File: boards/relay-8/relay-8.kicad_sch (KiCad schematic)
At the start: 8 parts, among them J1 Screw_Terminal_01x02, J2 USB_B_Micro, J3 Screw_Terminal_01x02, SW1 SW_Push, U1 ESP32-WROOM-32D, U2 MCP2200-I-MQ

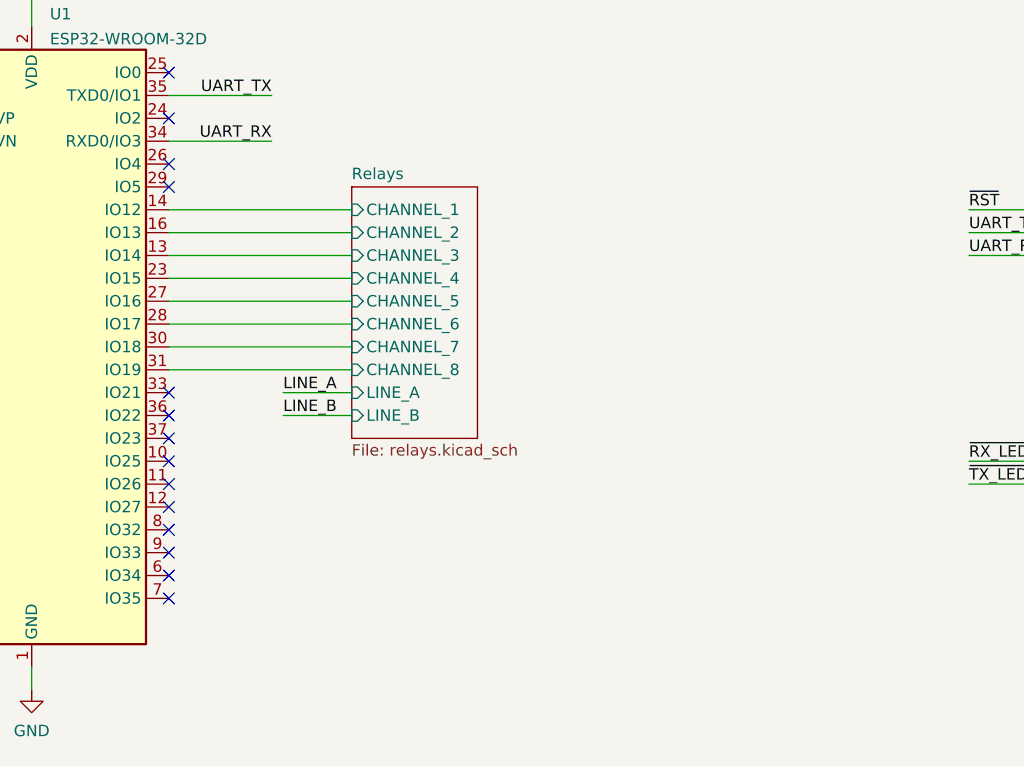
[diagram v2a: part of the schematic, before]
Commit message: Changed pin connections for relay channels
Signed-off-by: Computroniks <mnickson@sidingsmedia.com>
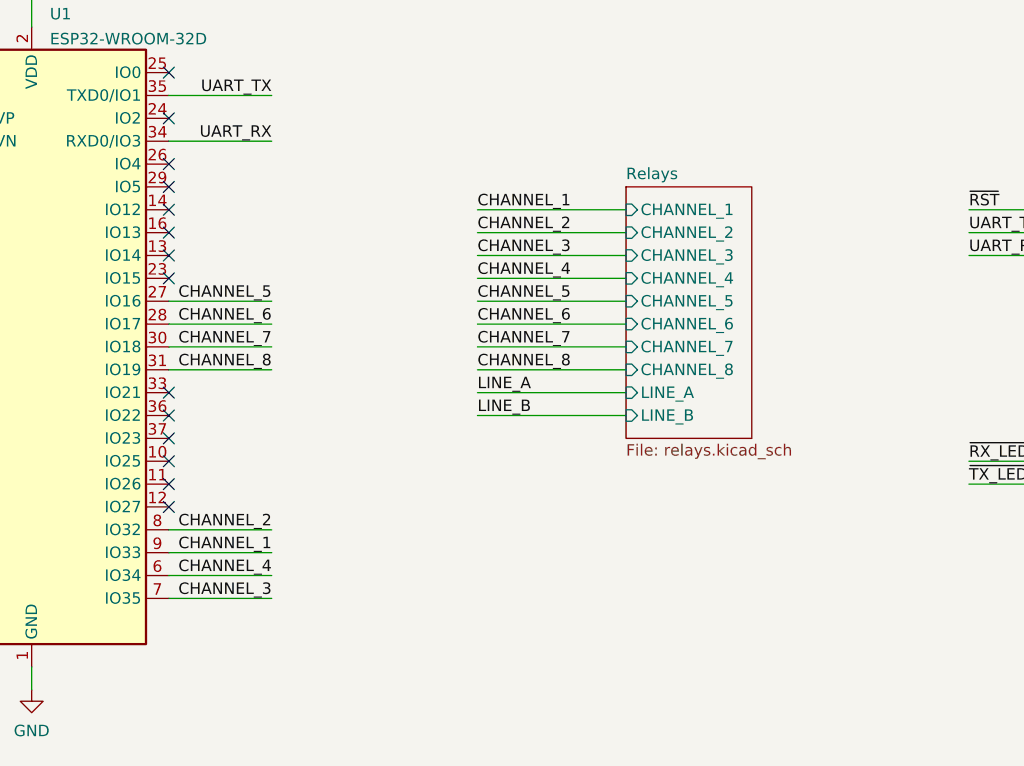
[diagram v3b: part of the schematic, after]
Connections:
- net CHANNEL_4: now reaches U1.6 (IO34)
- net CHANNEL_3: now reaches U1.7 (IO35)
- net CHANNEL_2: now reaches U1.8 (IO32)
- net CHANNEL_1: now reaches U1.9 (IO33)
- net Relays/CHANNEL_1: no longer names the net of U1.14 (IO12)
- net Relays/CHANNEL_2: no longer names the net of U1.16 (IO13)
- net Relays/CHANNEL_3: no longer names the net of U1.13 (IO14)
- net Relays/CHANNEL_4: no longer names the net of U1.23 (IO15)
- net Relays/CHANNEL_5 renamed CHANNEL_5
- net Relays/CHANNEL_6 renamed CHANNEL_6
- net Relays/CHANNEL_7 renamed CHANNEL_7
- net Relays/CHANNEL_8 renamed CHANNEL_8

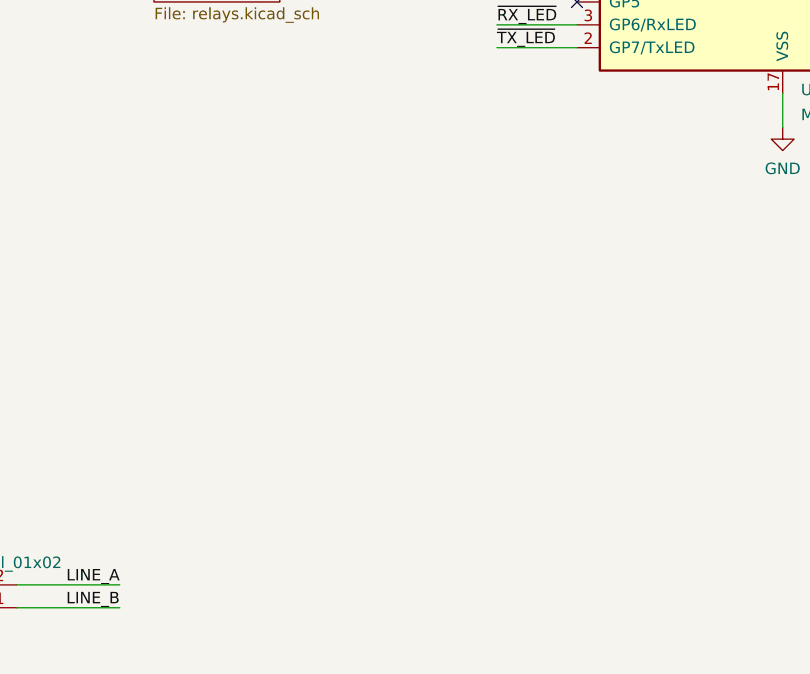
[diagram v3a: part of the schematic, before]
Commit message: Added Tx and Rx LEDs
Signed-off-by: Computroniks <mnickson@sidingsmedia.com>
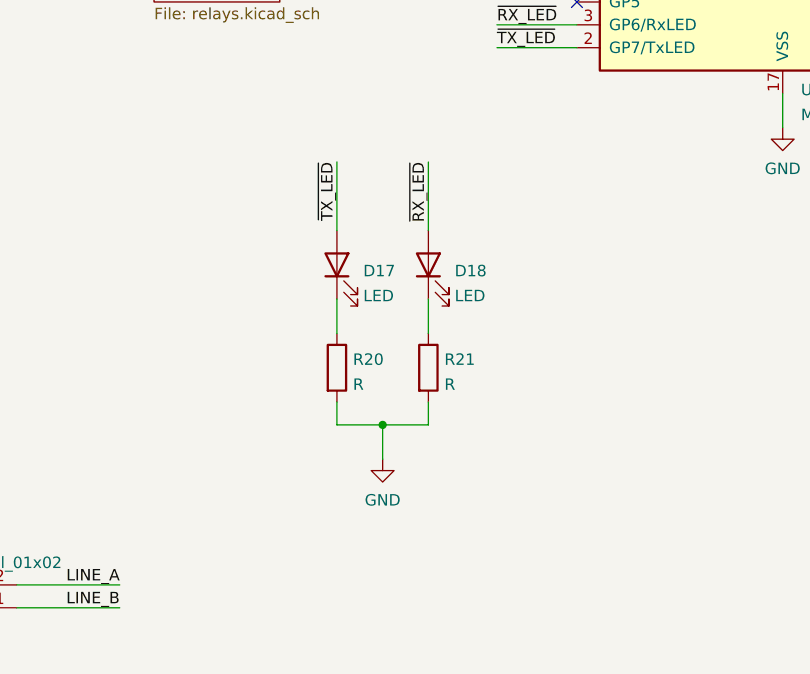
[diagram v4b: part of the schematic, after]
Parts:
- added D17, D18: LED, LED_SMD:LED_0805_2012Metric, symbol Device:LED
- added R20, R21: R, Resistor_SMD:R_0805_2012Metric, symbol Device:R
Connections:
- net GND: now also R20.2, R21.2
- net ~{RX_LED}: now also D18.2 (A)
- net ~{TX_LED}: now also D17.2 (A)
- new net: D17.1 (K), R20.1
- new net: D18.1 (K), R21.1
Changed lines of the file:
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@@
     (title "8 Channel Relay")
     (date "2022-03-20")
-    (rev "1.1.0")
+    (rev "1.1.1")
     (company "Matthew Nickson")
     (comment 1 "Licence: CC-BY-SA-4.0")
@@
   )
   (junction (at 40.64 76.2) (diameter 0) (color 0 0 0 0)
+  )
+  (junction (at 167.64 153.67) (diameter 0) (color 0 0 0 0)
   )
   (no_connect (at 60.96 96.52))
@@
     (stroke (width 0) (type default) (color 0 0 0 0))
   )
+  (wire (pts (xy 167.64 153.67) (xy 172.72 153.67))
+    (stroke (width 0) (type default) (color 0 0 0 0))
+  )
+  (wire (pts (xy 162.56 124.46) (xy 162.56 132.08))
+    (stroke (width 0) (type default) (color 0 0 0 0))
+  )
   (wire (pts (xy 214.63 72.39) (xy 214.63 76.2))
     (stroke (width 0) (type default) (color 0 0 0 0))
@@
     (stroke (width 0) (type default) (color 0 0 0 0))
   )
+  (wire (pts (xy 172.72 139.7) (xy 172.72 143.51))
+    (stroke (width 0) (type default) (color 0 0 0 0))
+  )
   (wire (pts (xy 96.52 176.53) (xy 107.95 176.53))
     (stroke (width 0) (type default) (color 0 0 0 0))
@@
     (stroke (width 0) (type default) (color 0 0 0 0))
   )
+  (wire (pts (xy 167.64 153.67) (xy 167.64 157.48))
+    (stroke (width 0) (type default) (color 0 0 0 0))
+  )
+  (wire (pts (xy 172.72 124.46) (xy 172.72 132.08))
+    (stroke (width 0) (type default) (color 0 0 0 0))
+  )
   (wire (pts (xy 40.64 66.04) (xy 50.8 66.04))
     (stroke (width 0) (type default) (color 0 0 0 0))
@@
     (stroke (width 0) (type default) (color 0 0 0 0))
   )
+  (wire (pts (xy 172.72 153.67) (xy 172.72 151.13))
+    (stroke (width 0) (type default) (color 0 0 0 0))
+  )
   (wire (pts (xy 125.73 88.9) (xy 142.24 88.9))
     (stroke (width 0) (type default) (color 0 0 0 0))
@@
     (stroke (width 0) (type default) (color 0 0 0 0))
   )
+  (wire (pts (xy 162.56 139.7) (xy 162.56 143.51))
+    (stroke (width 0) (type default) (color 0 0 0 0))
+  )
   (wire (pts (xy 91.44 91.44) (xy 102.87 91.44))
     (stroke (width 0) (type default) (color 0 0 0 0))
@@
     (stroke (width 0) (type default) (color 0 0 0 0))
   )
+  (wire (pts (xy 162.56 153.67) (xy 167.64 153.67))
+    (stroke (width 0) (type default) (color 0 0 0 0))
+  )
   (wire (pts (xy 43.18 179.07) (xy 43.18 181.61))
     (stroke (width 0) (type default) (color 0 0 0 0))
@@
     (stroke (width 0) (type default) (color 0 0 0 0))
   )
+  (wire (pts (xy 162.56 151.13) (xy 162.56 153.67))
+    (stroke (width 0) (type default) (color 0 0 0 0))
+  )
   (wire (pts (xy 180.34 109.22) (xy 189.23 109.22))
     (stroke (width 0) (type default) (color 0 0 0 0))
@@
     (effects (font (size 1.27 1.27)) (justify right bottom))
   )
+  (label "~{TX_LED}" (at 162.56 124.46 270)
+    (effects (font (size 1.27 1.27)) (justify right bottom))
+  )
   (label "USB_D-" (at 107.95 176.53 180)
     (effects (font (size 1.27 1.27)) (justify right bottom))
@@
   )
   (label "CHANNEL_7" (at 102.87 96.52 180)
+    (effects (font (size 1.27 1.27)) (justify right bottom))
+  )
+  (label "~{RX_LED}" (at 172.72 124.46 270)
     (effects (font (size 1.27 1.27)) (justify right bottom))
   )
@@
     (pin "9")
   )
+  (symbol (lib_id "power:GND") (at 167.64 157.48 0) (unit 1)
+    (in_bom yes) (on_board yes) (fields_autoplaced)
+    (property "Reference" "#PWR021" (id 0) (at 167.64 163.83 0)
+      (effects (font (size 1.27 1.27)) hide)
+    )
+    (property "Value" "GND" (id 1) (at 167.64 162.0425 0))
+    (property "Footprint" "" (id 2) (at 167.64 157.48 0)
+      (effects (font (size 1.27 1.27)) hide)
+    )
+    (property "Datasheet" "" (id 3) (at 167.64 157.48 0)
+      (effects (font (size 1.27 1.27)) hide)
+    )
+    (pin "1")
+  )
   (symbol (lib_id "Device:R") (at 40.64 60.96 0) (unit 1)
     (in_bom yes) (on_board yes)
@@
     )
     (property "Datasheet" "~" (id 3) (at 40.64 60.96 0)
+      (effects (font (size 1.27 1.27)) hide)
+    )
+    (pin "1")
+    (pin "2")
+  )
+  (symbol (lib_id "Device:R") (at 162.56 147.32 0) (unit 1)
+    (in_bom yes) (on_board yes) (fields_autoplaced)
+    (property "Reference" "R20" (id 0) (at 164.338 146.4115 0)
+      (effects (font (size 1.27 1.27)) (justify left))
+    )
+    (property "Value" "R" (id 1) (at 164.338 149.1866 0)
+      (effects (font (size 1.27 1.27)) (justify left))
+    )
+    (property "Footprint" "Resistor_SMD:R_0805_2012Metric" (id 2) (at 160.782 147.32 90)
+      (effects (font (size 1.27 1.27)) hide)
+    )
+    (property "Datasheet" "~" (id 3) (at 162.56 147.32 0)
+      (effects (font (size 1.27 1.27)) hide)
+    )
+    (pin "1")
+    (pin "2")
+  )
+  (symbol (lib_id "Device:LED") (at 162.56 135.89 90) (unit 1)
+    (in_bom yes) (on_board yes) (fields_autoplaced)
+    (property "Reference" "D17" (id 0) (at 165.481 136.569 90)
+      (effects (font (size 1.27 1.27)) (justify right))
+    )
+    (property "Value" "LED" (id 1) (at 165.481 139.3441 90)
+      (effects (font (size 1.27 1.27)) (justify right))
+    )
+    (property "Footprint" "LED_SMD:LED_0805_2012Metric" (id 2) (at 162.56 135.89 0)
+      (effects (font (size 1.27 1.27)) hide)
+    )
+    (property "Datasheet" "~" (id 3) (at 162.56 135.89 0)
       (effects (font (size 1.27 1.27)) hide)
     )
@@
     (pin "1")
   )
+  (symbol (lib_id "Device:R") (at 172.72 147.32 0) (unit 1)
+    (in_bom yes) (on_board yes) (fields_autoplaced)
+    (property "Reference" "R21" (id 0) (at 174.498 146.4115 0)
+      (effects (font (size 1.27 1.27)) (justify left))
+    )
+    (property "Value" "R" (id 1) (at 174.498 149.1866 0)
+      (effects (font (size 1.27 1.27)) (justify left))
+    )
+    (property "Footprint" "Resistor_SMD:R_0805_2012Metric" (id 2) (at 170.942 147.32 90)
+      (effects (font (size 1.27 1.27)) hide)
+    )
+    (property "Datasheet" "~" (id 3) (at 172.72 147.32 0)
+      (effects (font (size 1.27 1.27)) hide)
+    )
+    (pin "1")
+    (pin "2")
+  )
   (symbol (lib_id "power:GND") (at 40.64 78.74 0) (unit 1)
     (in_bom yes) (on_board yes)
@@
     )
     (pin "1")
+  )
+  (symbol (lib_id "Device:LED") (at 172.72 135.89 90) (unit 1)
+    (in_bom yes) (on_board yes) (fields_autoplaced)
+    (property "Reference" "D18" (id 0) (at 175.641 136.569 90)
+      (effects (font (size 1.27 1.27)) (justify right))
+    )
+    (property "Value" "LED" (id 1) (at 175.641 139.3441 90)
+      (effects (font (size 1.27 1.27)) (justify right))
+    )
+    (property "Footprint" "LED_SMD:LED_0805_2012Metric" (id 2) (at 172.72 135.89 0)
+      (effects (font (size 1.27 1.27)) hide)
+    )
+    (property "Datasheet" "~" (id 3) (at 172.72 135.89 0)
+      (effects (font (size 1.27 1.27)) hide)
+    )
+    (pin "1")
+    (pin "2")
   )
   (symbol (lib_id "power:+3V3") (at 212.09 68.58 0) (unit 1)
@@
       (reference "#PWR020") (unit 1) (value "GND") (footprint "")
     )
+    (path "/4f2d5c65-3158-47bb-8567-b2b7b18d83f0"
+      (reference "#PWR021") (unit 1) (value "GND") (footprint "")
+    )
     (path "/5f98f70e-ffd0-4082-8429-706e870aabe9/e6acf959-1004-4ea8-b14f-9f5a5417d645"
       (reference "#PWR0101") (unit 1) (value "+12V") (footprint "")
@@
       (reference "D16") (unit 1) (value "1N5819") (footprint "Diode_SMD:D_SMA")
     )
+    (path "/6b71e8ca-4b57-4517-aad7-9464ec88da7f"
+      (reference "D17") (unit 1) (value "LED") (footprint "LED_SMD:LED_0805_2012Metric")
+    )
+    (path "/ec83309a-09f3-4ac1-be38-ac793986a837"
+      (reference "D18") (unit 1) (value "LED") (footprint "LED_SMD:LED_0805_2012Metric")
+    )
     (path "/0c87e884-a22d-4e83-acb7-8a64f24b9e51"
       (reference "J1") (unit 1) (value "Screw_Terminal_01x02") (footprint "TerminalBlock:TerminalBlock_bornier-2_P5.08mm")
@@
       (reference "R19") (unit 1) (value "1K") (footprint "Resistor_SMD:R_0805_2012Metric")
     )
+    (path "/6396c417-3e83-4726-8802-cbbe0936d780"
+      (reference "R20") (unit 1) (value "R") (footprint "Resistor_SMD:R_0805_2012Metric")
+    )
+    (path "/ba4eb2c2-39bf-48d9-9310-1ca314f59aea"
+      (reference "R21") (unit 1) (value "R") (footprint "Resistor_SMD:R_0805_2012Metric")
+    )
     (path "/1da34727-da9f-4666-ab3e-a80afae32fa1"
